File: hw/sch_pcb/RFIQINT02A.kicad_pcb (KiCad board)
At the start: 2 copper layers, 40.1 x 60.5 mm, 40 parts, among them J1 SATA7-67491-1030, J2 RJ45_RJHSE-5384, J3 SATA7-67491-1030, J4 SATA7-67491-1030, J5 RJ45_RJHSE-5384, J6 HEADER_2x03_PARALLEL, J7 HEADER_2x04_PARALLEL, M1 HOLE, M2 HOLE, M3 HOLE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

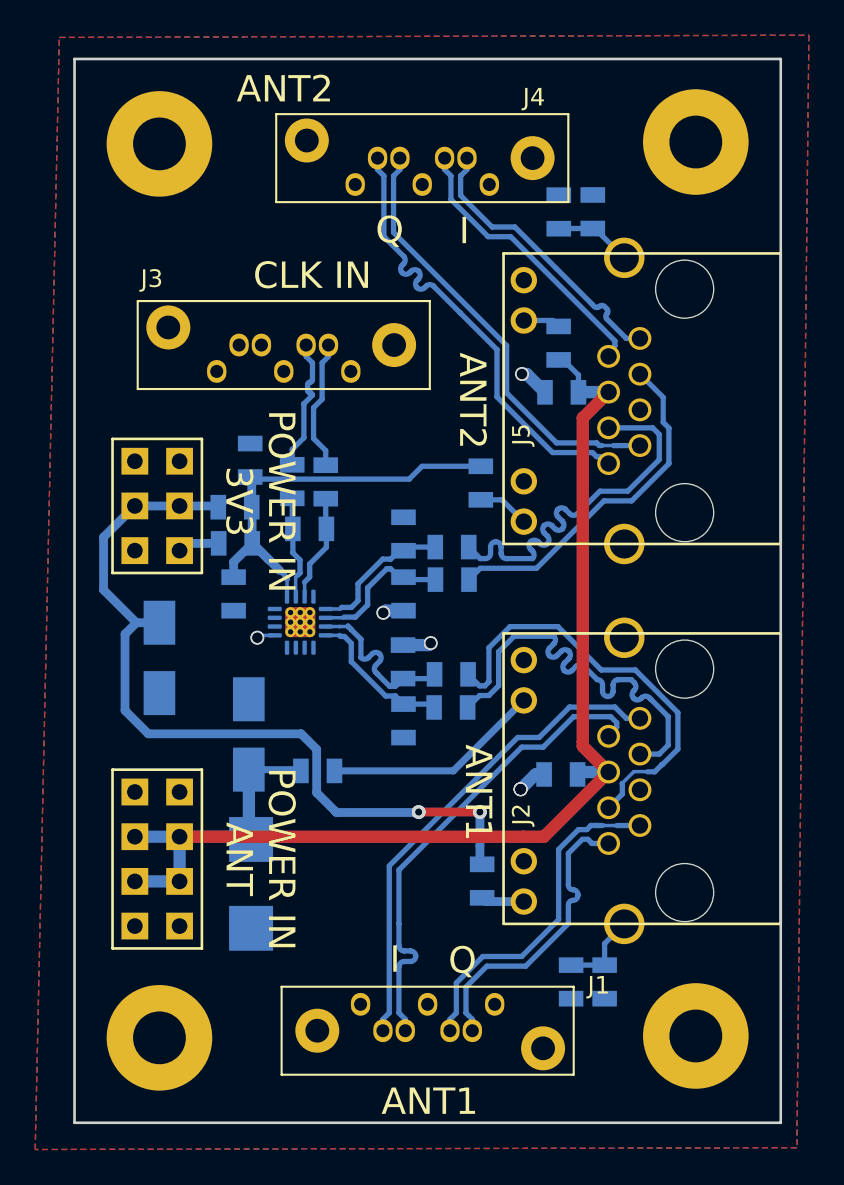
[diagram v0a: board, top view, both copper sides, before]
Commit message: Add grounding vias remove thermal relief at U1 grounding. #3.
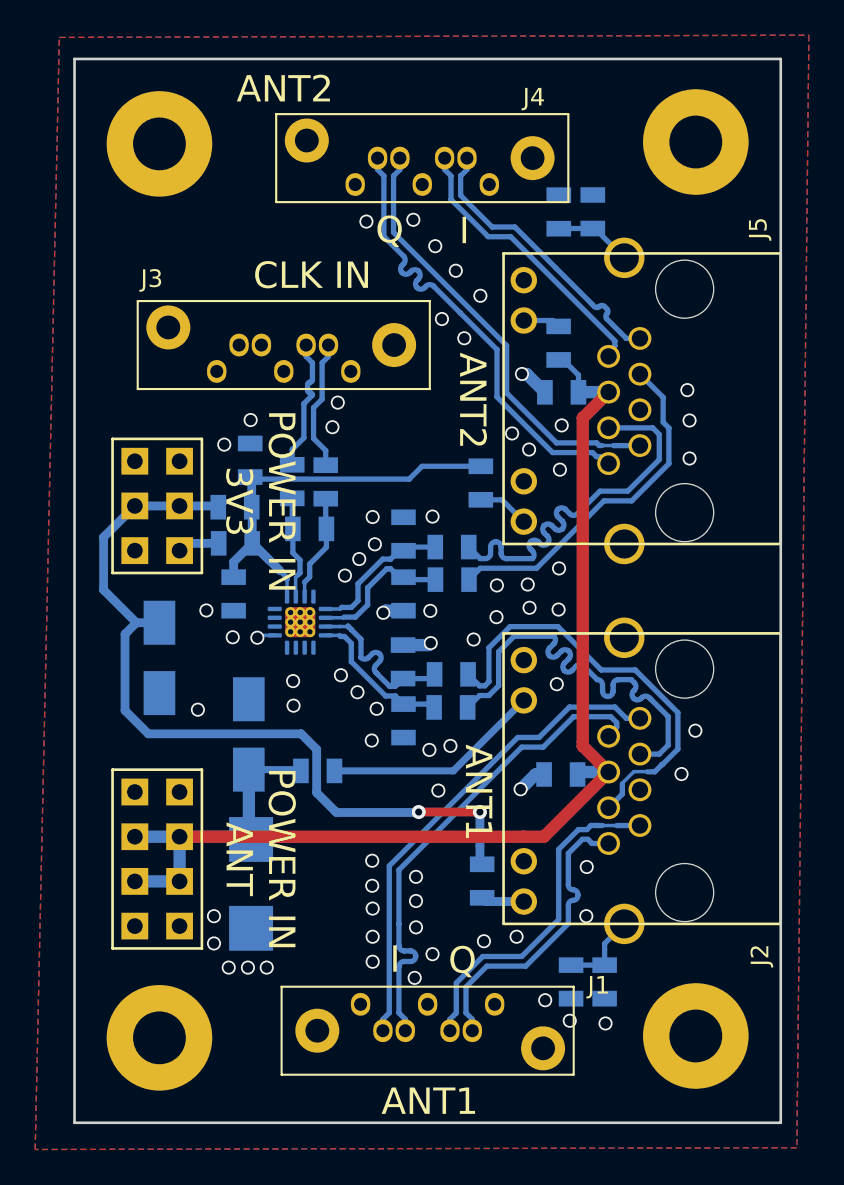
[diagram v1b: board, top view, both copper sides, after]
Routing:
- net GND: vias 6 -> 73

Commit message: Generating production data
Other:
- rule pad_to_mask_clearance: 0 -> 0.2
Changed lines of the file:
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@@
-(kicad_pcb (version 20210606) (generator pcbnew)
+(kicad_pcb (version 20210228) (generator pcbnew)
   (general
     (thickness 1.6)
@@
       (dielectric_constraints no)
     )
-    (pad_to_mask_clearance 0)
+    (pad_to_mask_clearance 0.2)
     (pcbplotparams
-      (layerselection 0x0000030_80000001)
+      (layerselection 0x00010e0_ffffffff)
       (disableapertmacros false)
       (usegerberextensions false)
@@
       (outputformat 1)
       (mirror false)
-      (drillshape 1)
+      (drillshape 0)
       (scaleselection 1)
-      (outputdirectory "")
+      (outputdirectory "../cam_profi/")
     )
   )
@@
     (pad "17" thru_hole circle locked (at 0.55 0) (size 0.6 0.6) (drill 0.3) (layers *.Cu)
       (net 2 "GND") (pinfunction "GND") (pintype "input") (zone_connect 2))
-    (pad "17" smd roundrect locked (at 0 0) (size 1.7 1.7) (layers "F.Cu") (roundrect_rratio 0.147059)
+    (pad "17" smd roundrect locked (at 0 0) (size 1.7 1.7) (layers "F.Cu") (roundrect_rratio 0.1470588235)
       (net 2 "GND") (pinfunction "GND") (pintype "input"))
     (pad "17" thru_hole circle locked (at 0 0) (size 0.6 0.6) (drill 0.3) (layers *.Cu)
       (net 2 "GND") (pinfunction "GND") (pintype "input") (zone_connect 2))
-    (pad "17" smd roundrect locked (at 0 0) (size 1.7 1.7) (layers "B.Cu" "B.Mask") (roundrect_rratio 0.147059)
+    (pad "17" smd roundrect locked (at 0 0) (size 1.7 1.7) (layers "B.Cu" "B.Mask") (roundrect_rratio 0.1470588235)
       (net 2 "GND") (pinfunction "GND") (pintype "input"))
     (pad "17" thru_hole circle locked (at 0 -0.55) (size 0.6 0.6) (drill 0.3) (layers *.Cu)
